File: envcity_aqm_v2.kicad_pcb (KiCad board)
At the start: 2 copper layers, 100 x 100 mm, 137 parts, among them IC1 DS1307ZN+, IC2 DMMT5401-7F, IC3 DMMT5401-7F, IC4 DMMT5401-7-F, IC6 ESP32-S2-SOLO-N4R2, J1 USB_B_Micro, J12 Conn_01x06_Male, J13 Conn_01x06_Male, J14 Conn_01x08_Pin, J15 Conn_01x02_Male, J16 Conn_01x02_Male, J2 Screw_Terminal_01x02, J3 Screw_Terminal_01x02, J4 Micro_SD_Card, J5 Conn_01x03_Male, J6 Conn_01x04_Male, J7 Conn_01x06_Pin, Q1 DMG2301L / DMP2045U, Q2 DMG2301L / DMP2045U, Q3 DMG2301L, Q4 DMG2301L, Q5 DMG2301L / DMP2045U, Q6 DMG2301L, Q7 DMN10H220L, Q8 DMN10H220L, SW1 RESET, SW2 BOOT, U1 TP4056, U10 RFM95W-915S2, U11 ADS1115IDGS, U2 USBLC6-2SC6, U3 MT3608, U4 MT3608, U5 LM2596S-5, U6 AP2112K-3.3, U7 DHT11, U8 AP2112K-3.3, U9 74HC4067DB, Y2 AB26TRB

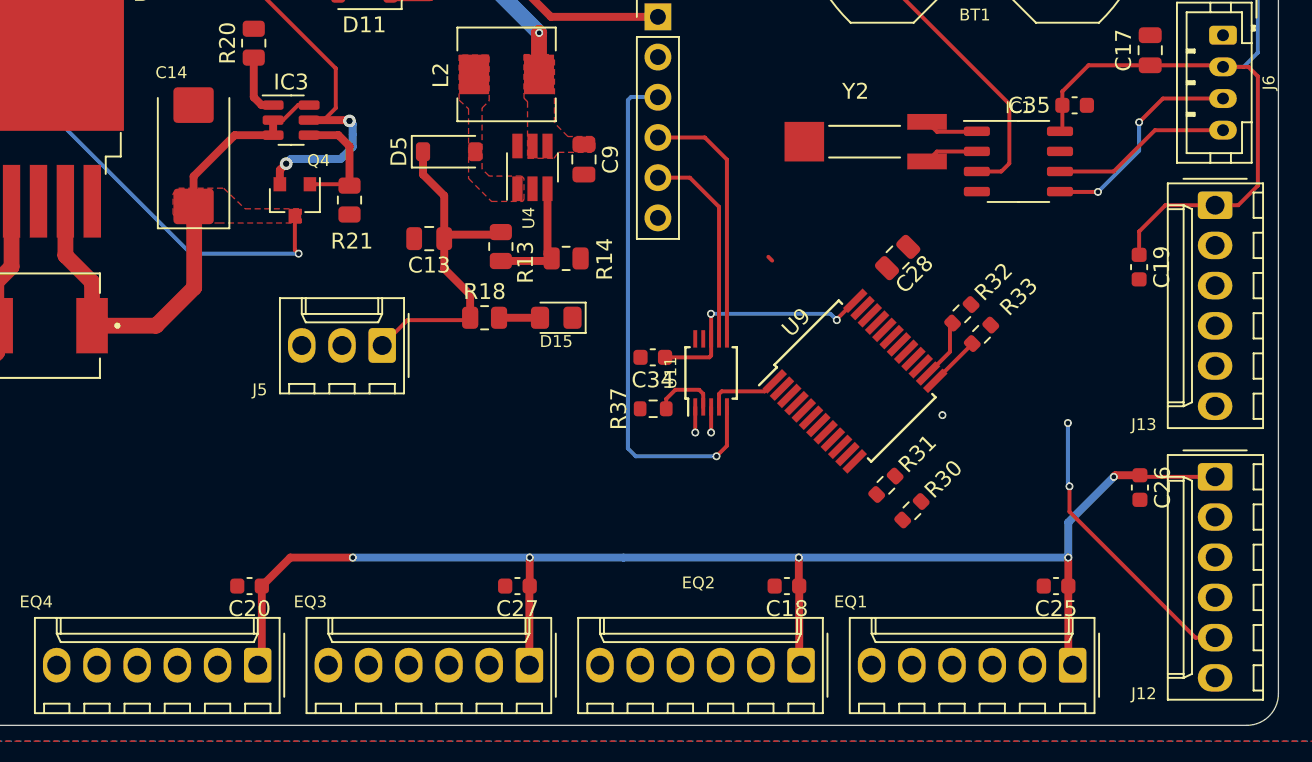
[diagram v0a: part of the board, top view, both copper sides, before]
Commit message: add 3dmodel cr2032 e algumas trilhas
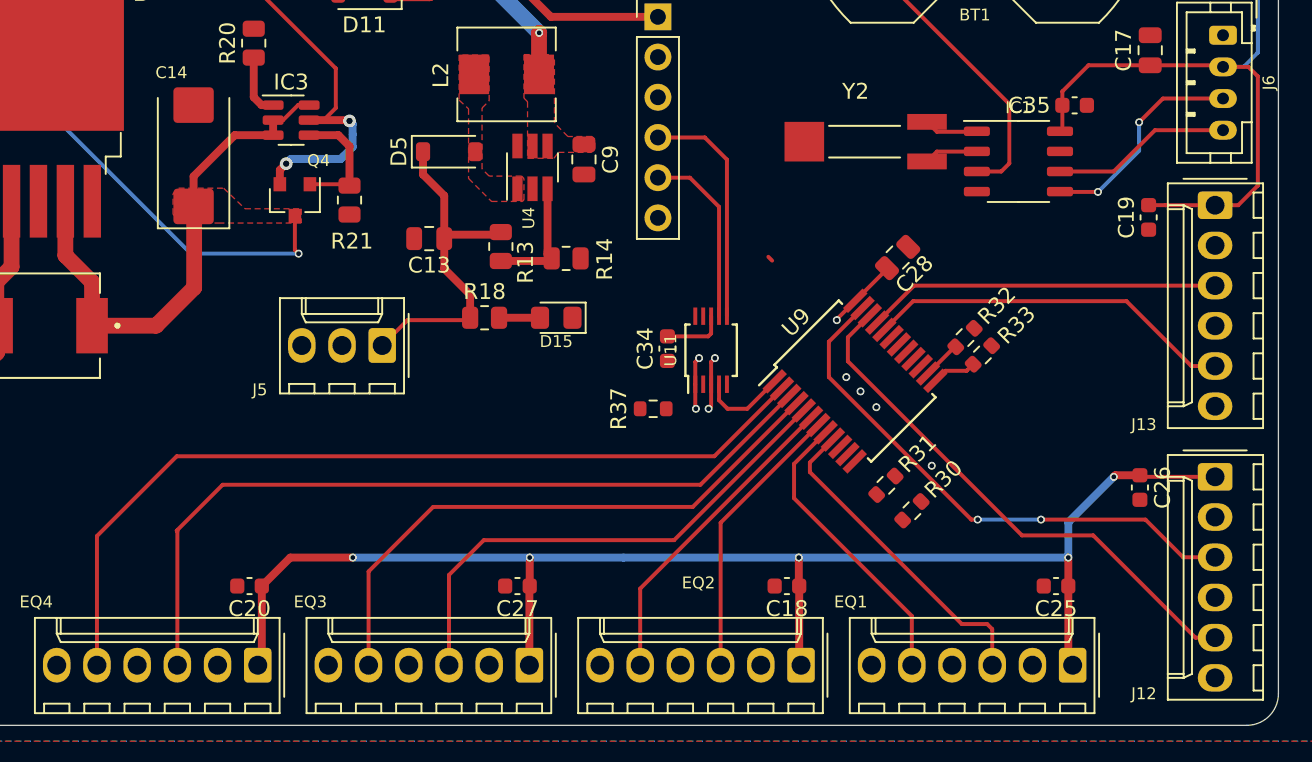
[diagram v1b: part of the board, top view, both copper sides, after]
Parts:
- moved C19 3.20 mm to (202.8, 127.9)
- moved R32 1.51 mm to (191.2, 135.5)
- moved U11 1.44 mm to (175.2, 136.3)
- moved R33 1.31 mm to (192.3, 136.6)
- moved C34 1.08 mm to (172.4, 136.2), turned to -90 degrees
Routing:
- net /I7: track 0.00 -> 55.3 mm
- net /I6: track 0.00 -> 50.7 mm
- net /I5: track 0.00 -> 37.4 mm
- net /I8: track 0.00 -> 34.4 mm, vias 0 -> 2
- net /AIN1: track 33.2 -> 0.00 mm, vias 1 -> 0
- net /I4: track 0.00 -> 32.4 mm
- net /I11: track 0.00 -> 23.3 mm
- net /I10: track 0.00 -> 22.3 mm
- net /I0: track 0.00 -> 20.6 mm
- net /I3: track 0.00 -> 20.1 mm
- net /I1: track 0.00 -> 18.6 mm
- net /I2: track 0.00 -> 17.7 mm
- net /I9: track 18.1 -> 33.9 mm, vias 2 -> 0
- net +5V: track 316.8 -> 307.1 mm, vias 15 -> 14
- net /ADS_ALERT: track 4.13 -> 0.00 mm
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
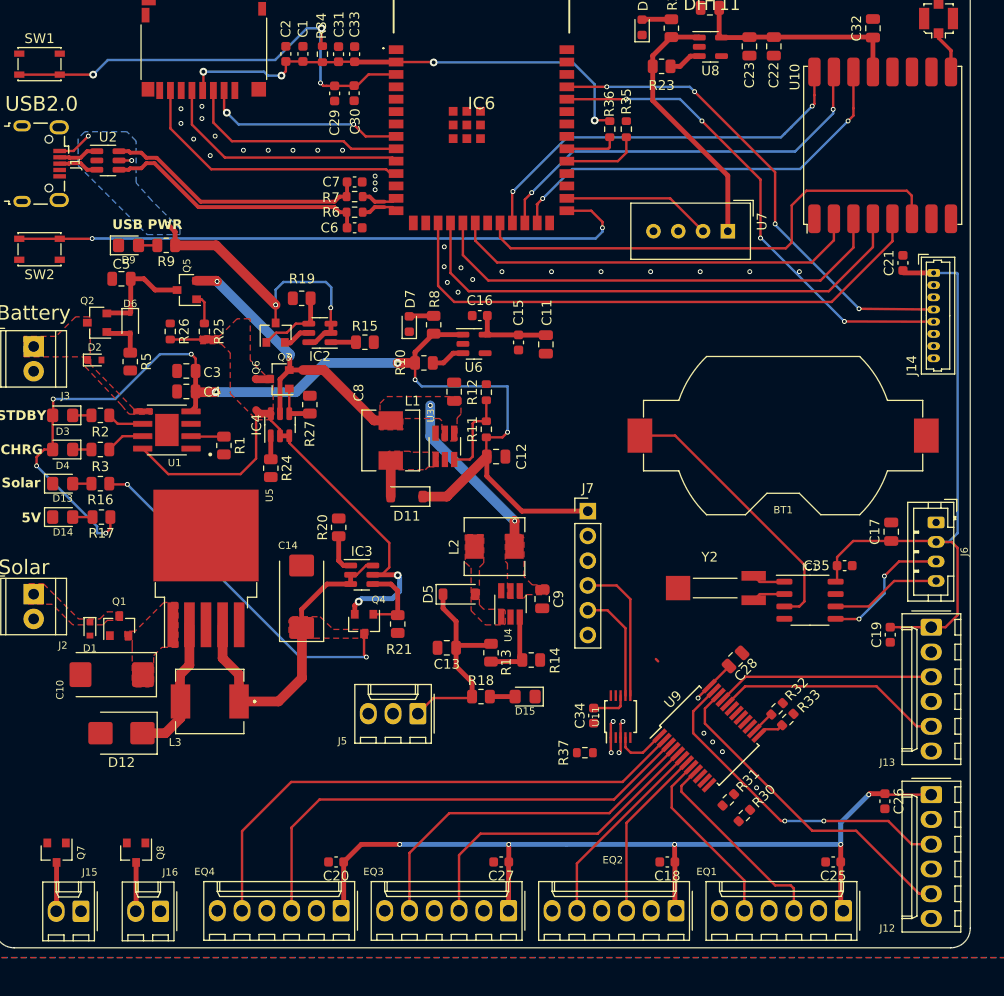
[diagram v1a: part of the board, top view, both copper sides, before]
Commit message: Alteracoes no roteamento
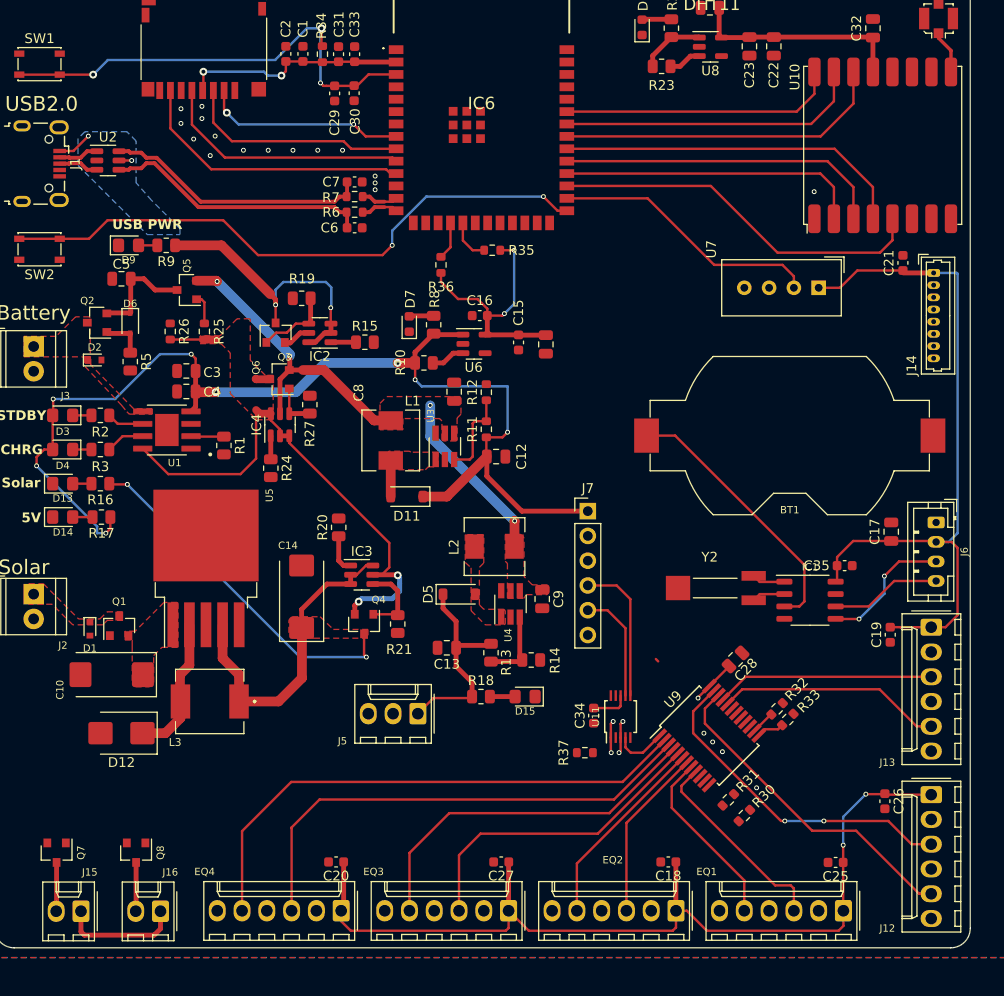
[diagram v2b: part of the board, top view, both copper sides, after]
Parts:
- moved R36 22.2 mm to (156.8, 90.0), turned to 90 degrees
- moved R35 18.5 mm to (162.0, 88.5), turned to 180 degrees
- moved U7 11.0 mm to (195.5, 92.3)
- moved BT1 0.68 mm to (192.5, 107.5)
- moved C25 0.25 mm to (197.2, 151.2)
- moved C18 0.10 mm to (180.1, 151.2)
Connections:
- net Net-(IC6-IO0) renamed /BOOT
- IC6 pad 12: unconnected-(IC6-IO8-Pad12) -> /IO8
- IC6 pad 15: unconnected-(IC6-IO3-Pad15) -> /FAN1
- IC6 pad 17: /RFM_CS -> /FAN2
- IC6 pad 18: /RFM_SCK -> /SCL
- IC6 pad 19: /RFM_MOSI -> /SDA
- IC6 pad 20: /RFM_MISO -> unconnected-(IC6-IO12-Pad20)
- IC6 pad 21: unconnected-(IC6-IO13-Pad21) -> /IO13
- IC6 pad 23: /RFM_DIO2 -> /IO21
- IC6 pad 24: /RFM_DIO1 -> /IO33
- IC6 pad 25: /RFM_DIO0 -> /IO34
- IC6 pad 29: unconnected-(IC6-IO36-Pad29) -> /RFM_CS
- IC6 pad 30: unconnected-(IC6-IO37-Pad30) -> /RFM_MISO
- IC6 pad 31: /SDA -> /RFM_MOSI
- IC6 pad 32: /SCL -> /RFM_SCK
- IC6 pad 33: unconnected-(IC6-IO40-Pad33) -> /RFM_DIO0
- IC6 pad 34: unconnected-(IC6-IO41-Pad34) -> /RFM_DIO1
- IC6 pad 35: unconnected-(IC6-IO42-Pad35) -> /RFM_DIO2
- IC6 pad 38: /FAN1 -> unconnected-(IC6-IO2-Pad38)
- IC6 pad 39: /FAN2 -> unconnected-(IC6-IO1-Pad39)
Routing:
- net /RFM_RST: track 51.4 -> 0.00 mm
- net /PMS_TX: track 50.6 -> 0.00 mm, vias 4 -> 0
- net /PMS_RX: track 50.3 -> 0.00 mm, vias 4 -> 0
- net /RFM_CS: track 58.9 -> 38.9 mm
- net /RFM_SCK: track 54.0 -> 36.3 mm
- net /RFM_MOSI: track 48.8 -> 33.7 mm
- net /RFM_DIO2: track 41.2 -> 28.4 mm, vias 2 -> 0
- net /DHT_PIN: track 15.4 -> 27.8 mm
- net /RFM_MISO: track 42.6 -> 31.2 mm
- net /RFM_DIO1: track 41.9 -> 31.3 mm, vias 2 -> 0
- net +3V3: track 57.9 -> 49.1 mm
- net /RFM_DIO0: track 42.6 -> 34.0 mm, vias 2 -> 0
- net +5V: track 307.1 -> 313.8 mm, vias 14 -> 11
- net /SDA: track 21.9 -> 18.2 mm
- net /BOOT: track 65.2 -> 62.4 mm
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
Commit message: add 3d model pms. add mais trilhas
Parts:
- removed D6: 5V, Diode_SMD:D_SOD-323
- removed R28, R29: 10k, Resistor_SMD:R_0805_2012Metric
- removed R5: 1K, Resistor_SMD:R_0805_2012Metric
- C17: footprint Capacitor_SMD:C_0805_2012Metric -> Capacitor_SMD:C_0603_1608Metric
- R1, R10, R15, R19, R20, R23, R24, R27, R8: footprint Resistor_SMD:R_0805_2012Metric -> Resistor_SMD:R_0603_1608Metric
- R30, R31, R32, R33: footprint Resistor_SMD:R_0603_1608Metric -> Resistor_SMD:R_0402_1005Metric_Pad0.72x0.64mm_HandSolder
- moved R30 75.3 mm to (174.2, 72.4), turned to 0 degrees
- moved R31 75.0 mm to (174.2, 70.8), turned to 0 degrees
- moved R32 70.0 mm to (174.2, 67.6), turned to 0 degrees
- moved R33 69.7 mm to (174.2, 69.3), turned to 0 degrees
- moved U7 34.8 mm to (162.4, 103.1), turned to 90 degrees
- moved C11 8.91 mm to (159.2, 94.9)
- moved C15 8.91 mm to (156.4, 94.7)
- moved C12 8.81 mm to (157.4, 102.4), turned to 90 degrees
- moved R24 8.67 mm to (133.9, 104.0), turned to 90 degrees
- moved D7 8.17 mm to (146.3, 92.1), turned to 0 degrees
- moved D11 8.16 mm to (146.8, 108.8)
- moved C16 8.04 mm to (153.4, 92.0)
- moved R8 7.85 mm to (148.8, 92.9)
- moved U6 7.85 mm to (153.0, 94.8)
- moved R11 7.72 mm to (154.9, 102.6)
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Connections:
- IC6 pad 18: /SCL -> /SDA
- IC6 pad 19: /SDA -> /SCL
- IC6 pad 20: unconnected-(IC6-IO12-Pad20) -> /IO12
- IC6 pad 23: /IO21 -> /DHT_PIN
- IC6 pad 25: /IO34 -> /PMS_TX
- IC6 pad 28: /DHT_PIN -> /PMS_RX
- IC6 pad 36: /PMS_TX -> unconnected-(IC6-RXD0-Pad36)
- IC6 pad 37: /PMS_RX -> unconnected-(IC6-TXD0-Pad37)
- IC6 pad 38: unconnected-(IC6-IO2-Pad38) -> /IO2
- IC6 pad 39: unconnected-(IC6-IO1-Pad39) -> /IO1
- Q2 pad 1: Net-(D6-A) -> GND
- R35 pad 2: /SDA -> /SCL
- R36 pad 2: /SCL -> /SDA
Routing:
- net /SCL: track 15.3 -> 102.7 mm, vias 0 -> 2
- net +5V: track 313.8 -> 394.7 mm
- net /SDA: track 18.2 -> 89.6 mm
- net /PMS_TX: track 0.00 -> 45.8 mm
- net /PMS_RX: track 0.00 -> 42.3 mm
- net +3V3: track 49.1 -> 73.9 mm, vias 4 -> 6
- net Vbat_protected: track 11.2 -> 0.00 mm
- net /DHT_PIN: track 27.8 -> 17.8 mm, vias 0 -> 1
- net /AIN0: track 5.47 -> 0.00 mm
- net Net-(D6-A): track 4.56 -> 0.00 mm
- net Vexternal: track 63.7 -> 67.9 mm
- net Vusb: track 35.1 -> 31.8 mm, vias 4 -> 5
- net Vsys: track 49.8 -> 52.9 mm
- net /S3: track 2.83 -> 0.00 mm
- net /S2: track 2.45 -> 0.00 mm
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- added copper zone on F.Cu, net +5V
- added copper zone on F.Cu, net Vbat_protected
- removed copper zone on F.Cu, net Vexternal

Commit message: add trilhas
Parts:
- R13, R14, R16, R17, R18, R2, R3: footprint Resistor_SMD:R_0805_2012Metric -> Resistor_SMD:R_0603_1608Metric
- moved R32 34.8 mm to (143.8, 50.8)
- moved J5 3.18 mm to (157.0, 134.2)
- moved R18 2.34 mm to (161.5, 132.0)
- moved D15 2.25 mm to (165.5, 132.0)
- moved R25 2.21 mm to (131.8, 94.8)
- moved R26 1.35 mm to (128.8, 95.5), turned to 0 degrees
- moved R14 1.27 mm to (165.8, 129.2)
- moved U1 0.66 mm to (128.0, 106.9)
- moved R13 0.58 mm to (161.6, 129.2), turned to 0 degrees
- moved C30 0.53 mm to (147.5, 72.0)
- moved C29 0.42 mm to (145.8, 72.0)
- moved C3 0.38 mm to (129.6, 100.9)
- moved C4 0.38 mm to (129.6, 103.0)
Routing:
- net +9V: track 21.8 -> 16.8 mm
- net Vexternal: track 67.9 -> 64.2 mm
- net Net-(Q5-G): track 5.45 -> 3.24 mm
- net /BST_FB_9V: track 7.79 -> 5.70 mm
- net Net-(U1-~{STDBY}): track 3.79 -> 3.13 mm
- net Net-(U1-~{CHRG}): track 4.00 -> 3.34 mm
- net Net-(D15-A): track 2.59 -> 2.06 mm
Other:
- board text added: "CHG"
- board text added: "STBY"
- board text added: "Sol."
- board text removed: "CHRG"
- board text removed: "STDBY"
